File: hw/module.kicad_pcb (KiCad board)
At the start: 2 copper layers, 30 x 30 mm, 43 parts, among them Q1 MUN 2211, U1 CFPS-39, U2 CFPS-39, U3 74LVC1G125, U4 74 LVC 1G3157GW,125, U5 MAX919, U6 STM32L010F4P6, U7 BAS70-7-F, U8 SS39ET

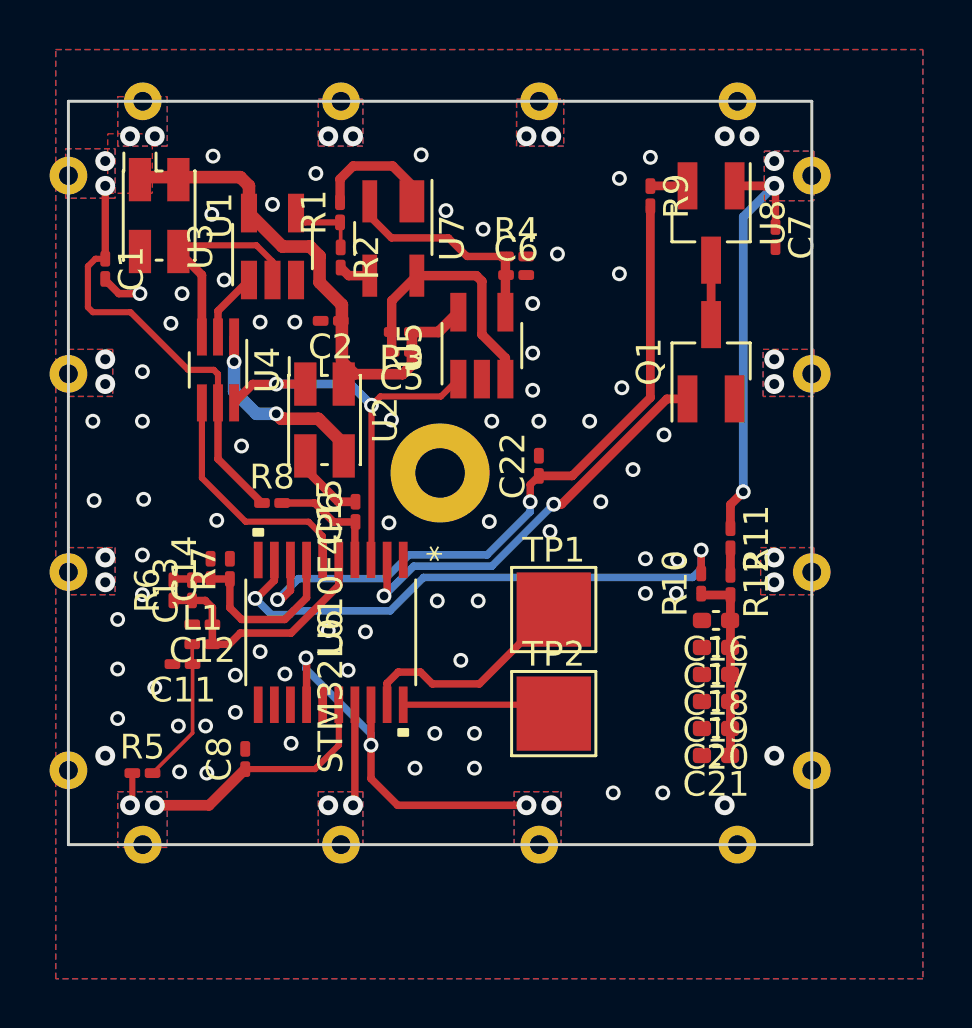
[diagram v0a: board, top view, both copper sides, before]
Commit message: 0603 passives
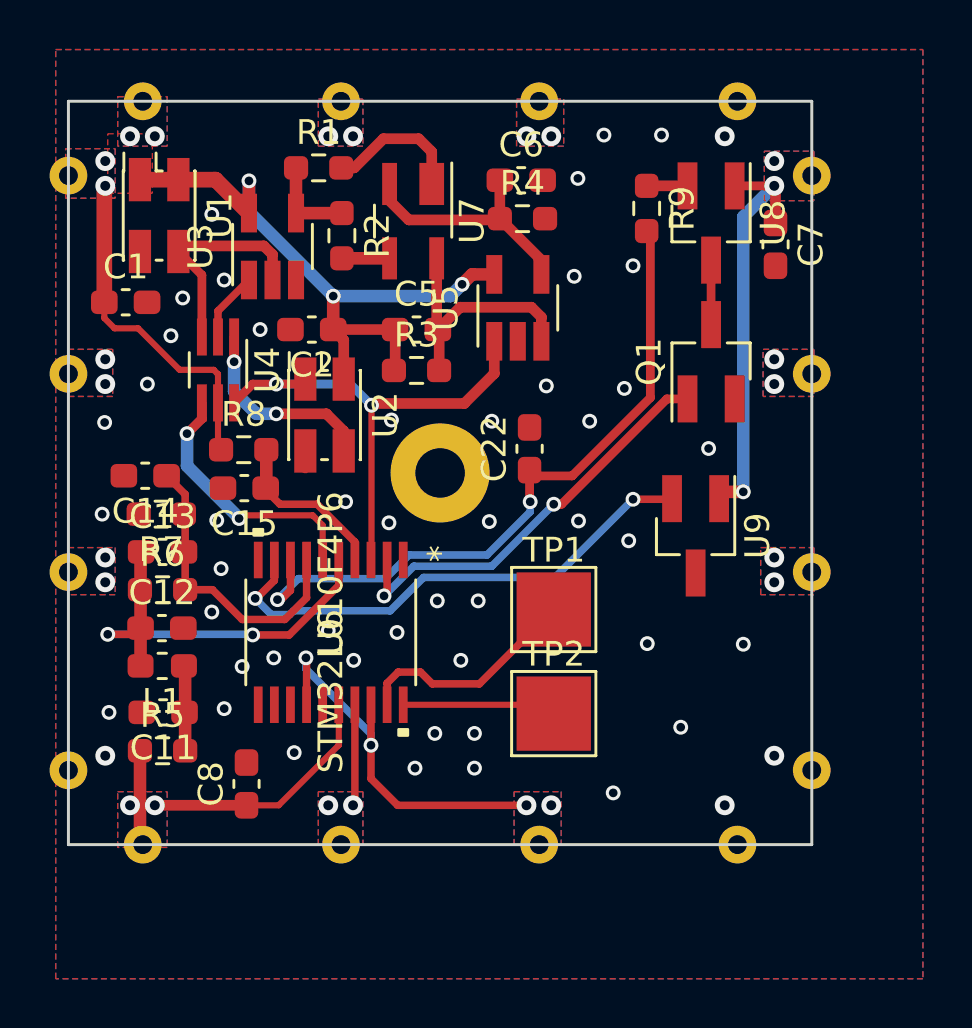
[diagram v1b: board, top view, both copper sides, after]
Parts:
- removed C16, C17, C18, C19, C20, C21: 4u7, Capacitor_SMD:C_0402_1005Metric_Pad0.74x0.62mm_HandSolder
- removed R10, R11, R12: 150k, Resistor_SMD:R_0201_0603Metric_Pad0.64x0.40mm_HandSolder
- added U9: LM 61BIM3, Package_TO_SOT_SMD:SOT-23_Handsoldering, F.Cu at (68.3, 59.6)
- C1, C11, C12, C13, C14, C15, C2, C22, C5, C6, C7, C8: footprint Capacitor_SMD:C_0201_0603Metric_Pad0.64x0.40mm_HandSolder -> Capacitor_SMD:C_0603_1608Metric_Pad1.08x0.95mm_HandSolder
- L1: footprint Inductor_SMD:L_0201_0603Metric_Pad0.64x0.40mm_HandSolder -> Inductor_SMD:L_0603_1608Metric_Pad1.05x0.95mm_HandSolder
- R1, R2, R3, R4, R5, R6, R7, R8, R9: footprint Resistor_SMD:R_0201_0603Metric_Pad0.64x0.40mm_HandSolder -> Resistor_SMD:R_0603_1608Metric_Pad0.98x0.95mm_HandSolder
- moved C14 4.59 mm to (46.1, 57.2), turned to 180 degrees
- moved C15 4.59 mm to (50.1, 57.7), turned to 180 degrees
- moved C6 3.83 mm to (61.3, 45.3)
- moved R7 3.54 mm to (46.8, 58.8), turned to 180 degrees
- moved R8 2.44 mm to (50.1, 56.1)
- moved U5 2.10 mm to (61.1, 50.4)
- moved C11 2.10 mm to (46.8, 66.8)
- moved R1 1.99 mm to (53.1, 44.8), turned to 0 degrees
- moved C13 1.95 mm to (46.8, 60.3), turned to 0 degrees
- moved L1 1.84 mm to (46.8, 64.9), turned to 180 degrees
- moved R3 1.66 mm to (57.1, 53.0), turned to 0 degrees
- moved C12 1.64 mm to (46.8, 63.4), turned to 0 degrees
- moved C1 1.58 mm to (45.3, 50.2), turned to 0 degrees
- moved R4 1.55 mm to (61.3, 46.8)
- moved R5 1.21 mm to (46.8, 68.3)
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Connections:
- U6 pad 9: /Cap_experiment -> /Temp
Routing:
- net /Cap_experiment: track 22.6 -> 0.00 mm, vias 2 -> 0
- net /Temp: track 0.00 -> 20.9 mm, vias 0 -> 2
- net Net-(C16-Pad1): track 7.69 -> 0.00 mm
- net +3.3VA: track 10.3 -> 17.2 mm, vias 0 -> 2
- net GND: track 7.59 -> 3.34 mm, vias 74 -> 50
- net +3.3V: track 67.7 -> 71.9 mm, vias 9 -> 12
- net /half_vref: track 8.64 -> 12.2 mm
- net /OSC_STAT: track 17.6 -> 20.5 mm
- net Net-(C11-Pad1): track 5.88 -> 3.45 mm
- net Net-(C15-Pad1): track 4.82 -> 6.72 mm
- net Net-(R11-Pad2): track 1.07 -> 0.00 mm
- net /OSC: track 9.85 -> 10.8 mm, vias 0 -> 2
- net Net-(R1-Pad1): track 2.95 -> 3.67 mm
- net Net-(R1-Pad2): track 5.02 -> 5.65 mm
- net Net-(R2-Pad2): track 1.31 -> 1.93 mm
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
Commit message: Add the last wire
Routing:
- net GND: track 3.34 -> 5.51 mm
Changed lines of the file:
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@@
   (segment (start 52.6 65) (end 55.224998 67.624998) (width 0.3048) (layer "B.Cu") (net 2))
   (segment (start 49.05 51.6) (end 49.05 50.55) (width 0.3048) (layer "F.Cu") (net 3))
+  (segment (start 45.9 48.15) (end 45.9 49.9125) (width 0.4318) (layer "F.Cu") (net 3))
   (segment (start 49.05 50.55) (end 50.3 49.3) (width 0.3048) (layer "F.Cu") (net 3))
   (segment (start 52.575 56.925) (end 52.575 56.4) (width 0.3556) (layer "F.Cu") (net 3))
+  (segment (start 45.9 49.9125) (end 46.1875 50.2) (width 0.4318) (layer "F.Cu") (net 3))
   (via (at 54.2 58.25) (size 0.6) (drill 0.35) (layers "F.Cu" "B.Cu") (free) (net 3))
   (via (at 54.525 64.65) (size 0.6) (drill 0.35) (layers "F.Cu" "B.Cu") (free) (net 3))
